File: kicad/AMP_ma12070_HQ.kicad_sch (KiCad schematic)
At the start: 21 parts

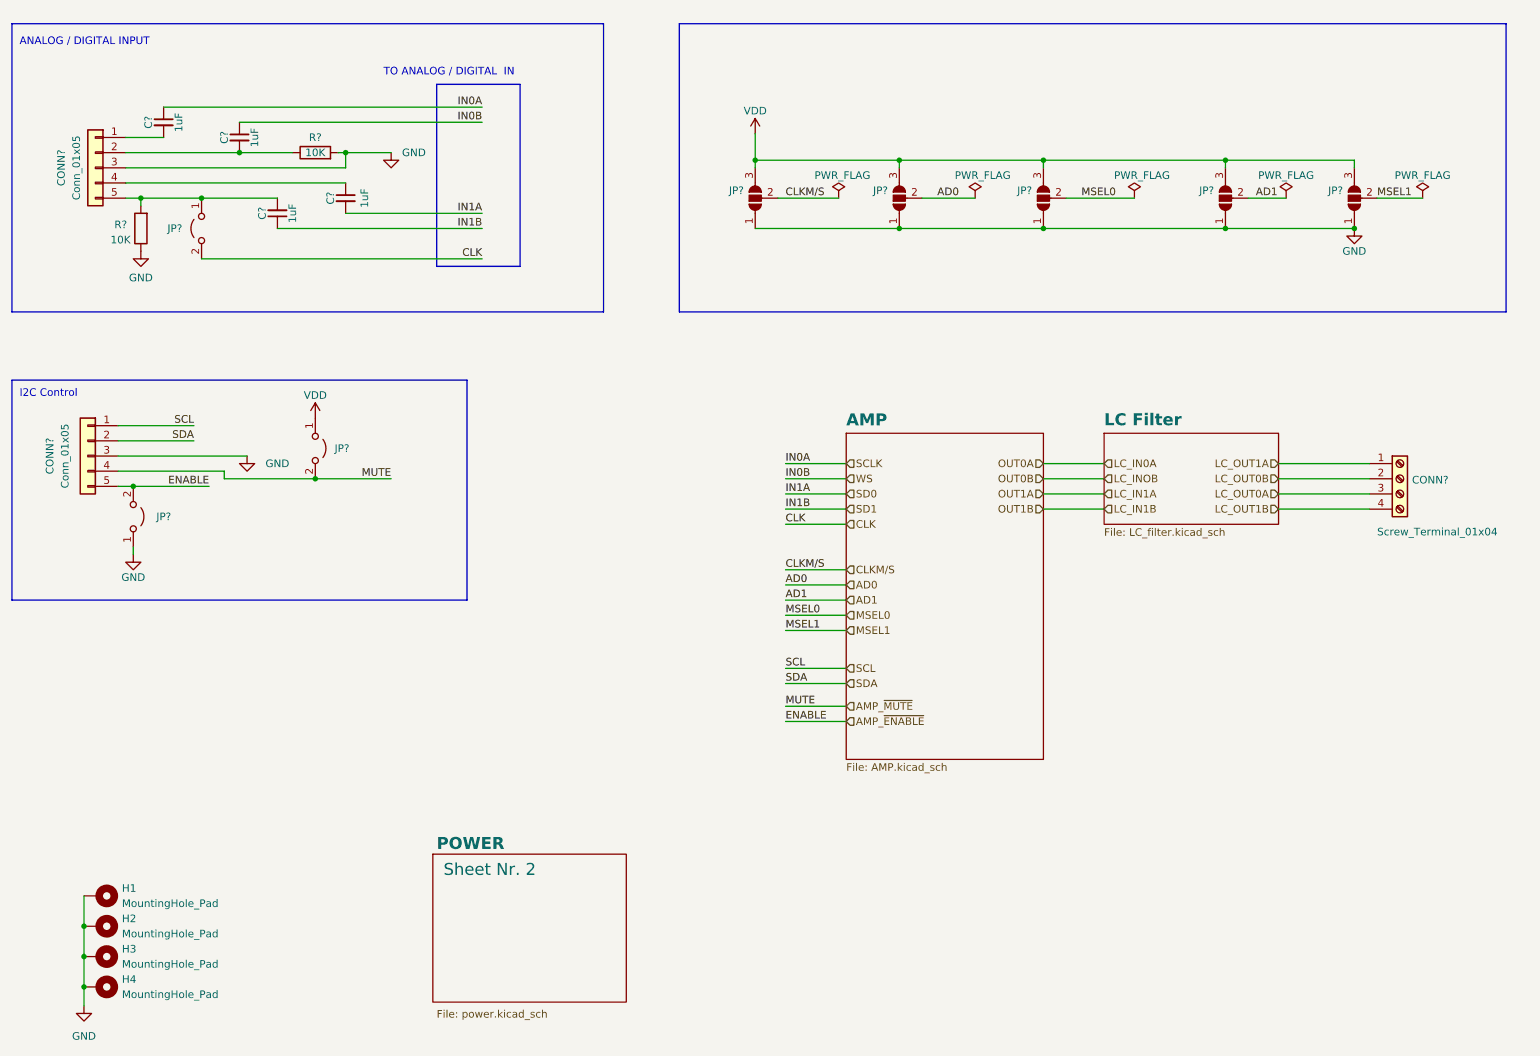
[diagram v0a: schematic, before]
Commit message: changed schematic layout
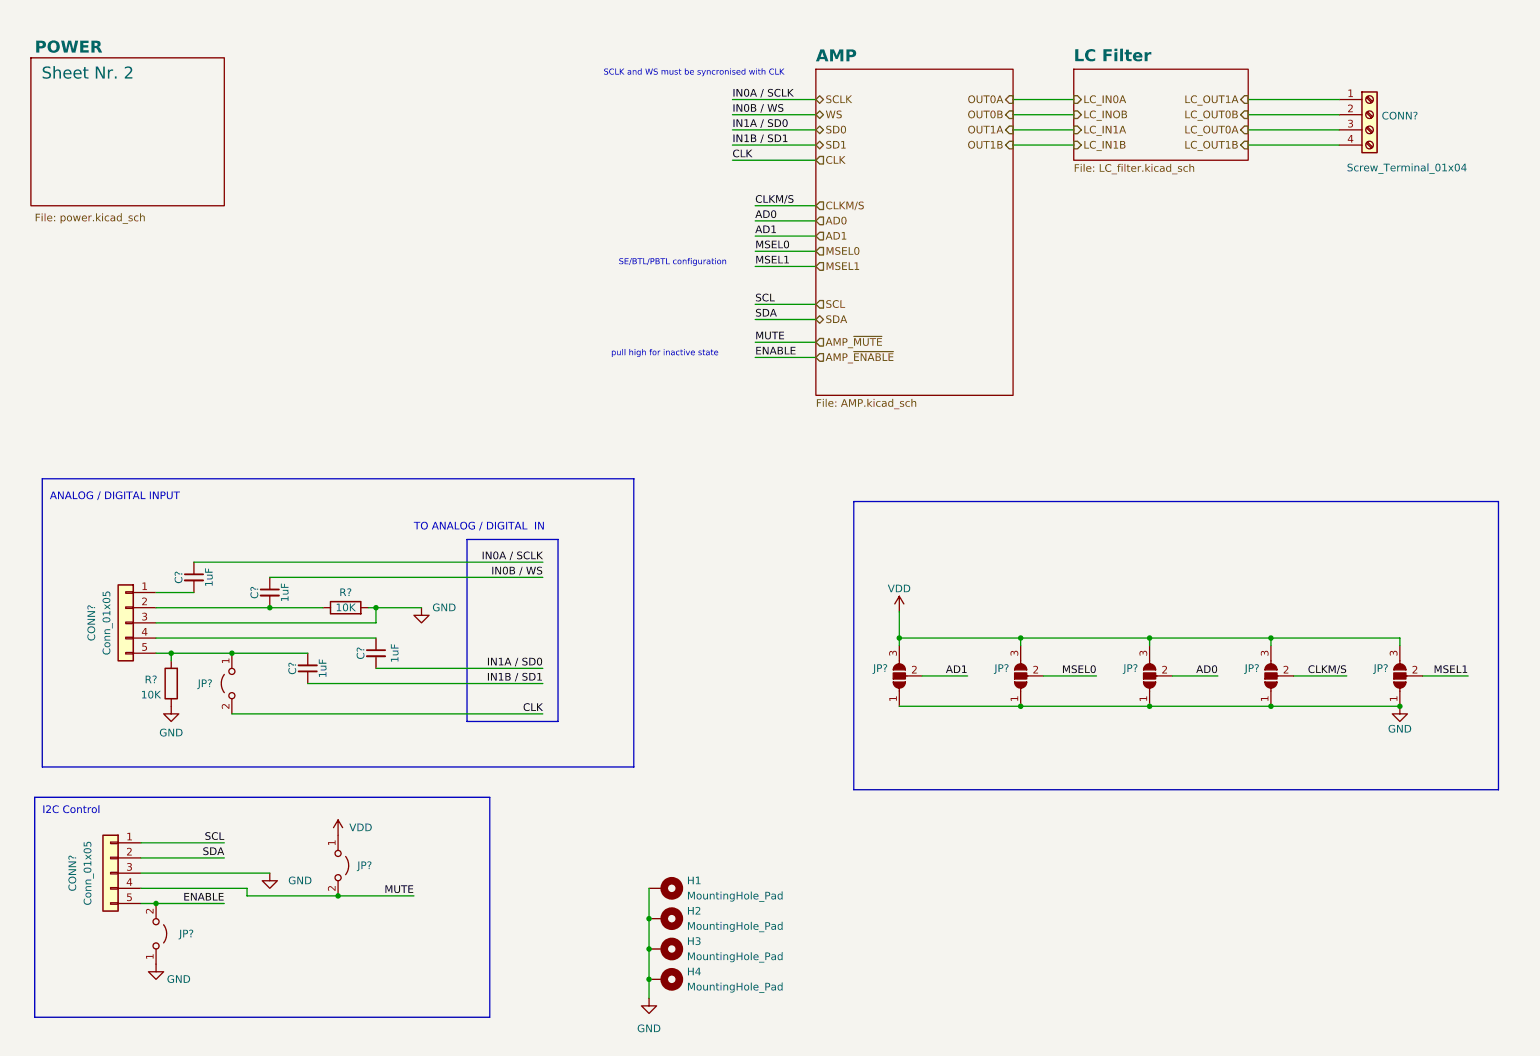
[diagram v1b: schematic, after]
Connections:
- net AD0: now also JP?.2 (C); no longer JP?.2 (C)
- net AD1: now also JP?.2 (C); no longer JP?.2 (C)
- net CLKM/S: now also JP?.2 (C); no longer JP?.2 (C)
- net MSEL0: now also JP?.2 (C); no longer JP?.2 (C)
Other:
- note added: "SCLK and WS must be syncronised with CLK"
- note added: "SE/BTL/PBTL configuration"
- note added: "pull high for inactive state"
- moved on the sheet: C?, CONN?, H1, H2, H3, H4, JP?, R?

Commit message: ongoing work
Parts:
- removed C? (x4): 1uF, Capacitor_SMD:C_1206_3216Metric, symbol Device:C_Small
- removed JP? (x5): SolderJumper_3_Open, Jumper:SolderJumper-3_P1.3mm_Open_Pad1.0x1.5mm, symbol Jumper:SolderJumper_3_Open
- removed JP?: SolderJumper_2_Open, Connector_PinHeader_2.54mm:PinHeader_1x02_P2.54mm_Vertical, symbol Jumper:Jumper_2_Open
- removed R? (x2): 10K, Resistor_SMD:R_1206_3216Metric, symbol Device:R
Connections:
- net IN0B: now reaches CONN?.2 (Pin_2)
- net IN1A: now reaches CONN?.4 (Pin_4)
- net IN1B: now reaches CONN?.5 (Pin_5)
- net IN0A: now reaches CONN?.1 (Pin_1)
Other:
- note removed: "SE/BTL/PBTL configuration"
- note removed: "TO ANALOG / DIGITAL IN"
- note removed: "pull high for inactive state"
- moved on the sheet: CONN?, JP?

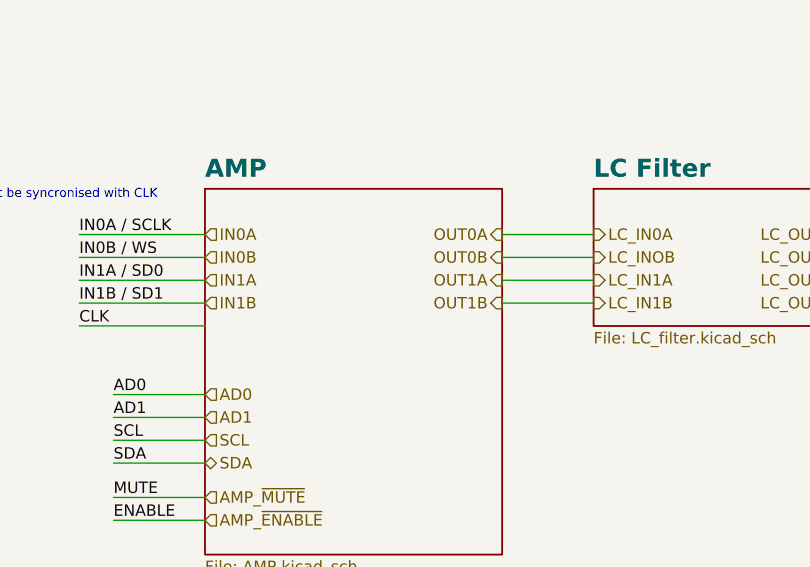
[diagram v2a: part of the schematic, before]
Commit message: generated pdf schematic
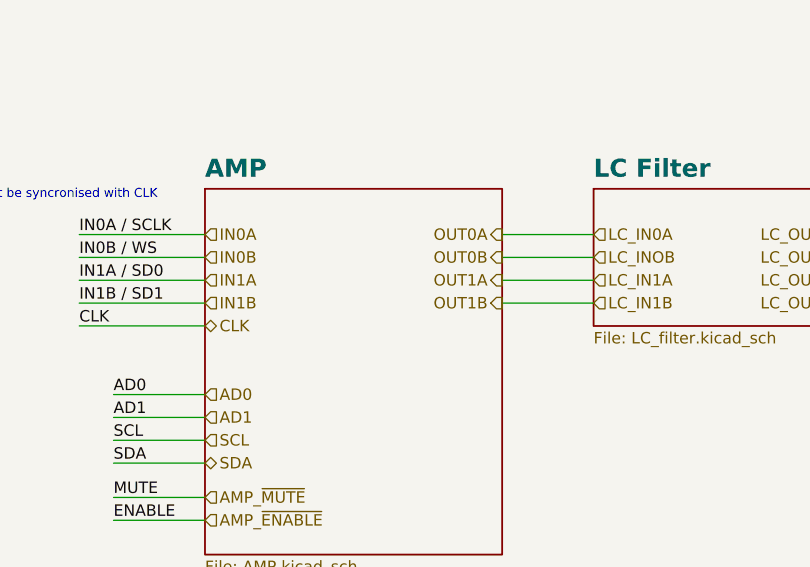
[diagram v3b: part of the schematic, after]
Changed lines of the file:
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@@
     (effects (font (size 1.27 1.27)) (justify right))
   )
-  (hierarchical_label "LC_INOB" (shape output) (at 194.31 90.17 0)
+  (hierarchical_label "LC_INOB" (shape input) (at 194.31 90.17 0)
     (effects (font (size 1.27 1.27)) (justify left))
   )
@@
     (effects (font (size 1.27 1.27)) (justify left))
   )
-  (hierarchical_label "LC_IN1B" (shape output) (at 194.31 95.25 0)
+  (hierarchical_label "CLK" (shape bidirectional) (at 151.13 97.79 0)
+    (effects (font (size 1.27 1.27)) (justify left))
+  )
+  (hierarchical_label "LC_IN1B" (shape input) (at 194.31 95.25 0)
     (effects (font (size 1.27 1.27)) (justify left))
   )
@@
     (effects (font (size 1.27 1.27)) (justify left))
   )
-  (hierarchical_label "LC_IN1A" (shape output) (at 194.31 92.71 0)
+  (hierarchical_label "LC_IN1A" (shape input) (at 194.31 92.71 0)
     (effects (font (size 1.27 1.27)) (justify left))
   )
@@
     (effects (font (size 1.27 1.27)) (justify right))
   )
-  (hierarchical_label "LC_IN0A" (shape output) (at 194.31 87.63 0)
+  (hierarchical_label "LC_IN0A" (shape input) (at 194.31 87.63 0)
     (effects (font (size 1.27 1.27)) (justify left))
   )
